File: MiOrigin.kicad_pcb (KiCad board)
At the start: 2 copper layers, 56.3 x 98 mm, 63 parts, among them J2 USB_C_Receptacle, J3 Micro_SD_Card, J4 CONN_02JST-PTH-2, J5 DB9_Male_MountingHoles, Q1 PMBT3904YS, Q2 DMG2305UX-13, Q5 DMG2305UX-13, U1 ESP32-WROOM-32U, U2 CH340C, U3 MCP73811T-420I-OT, U4 3.5-TFT-LCD-SPI, U5 AP2112K-3.3, U6 MAX1704X, U7 SN74LVC125ADBR_(Units), U8 MAX3232

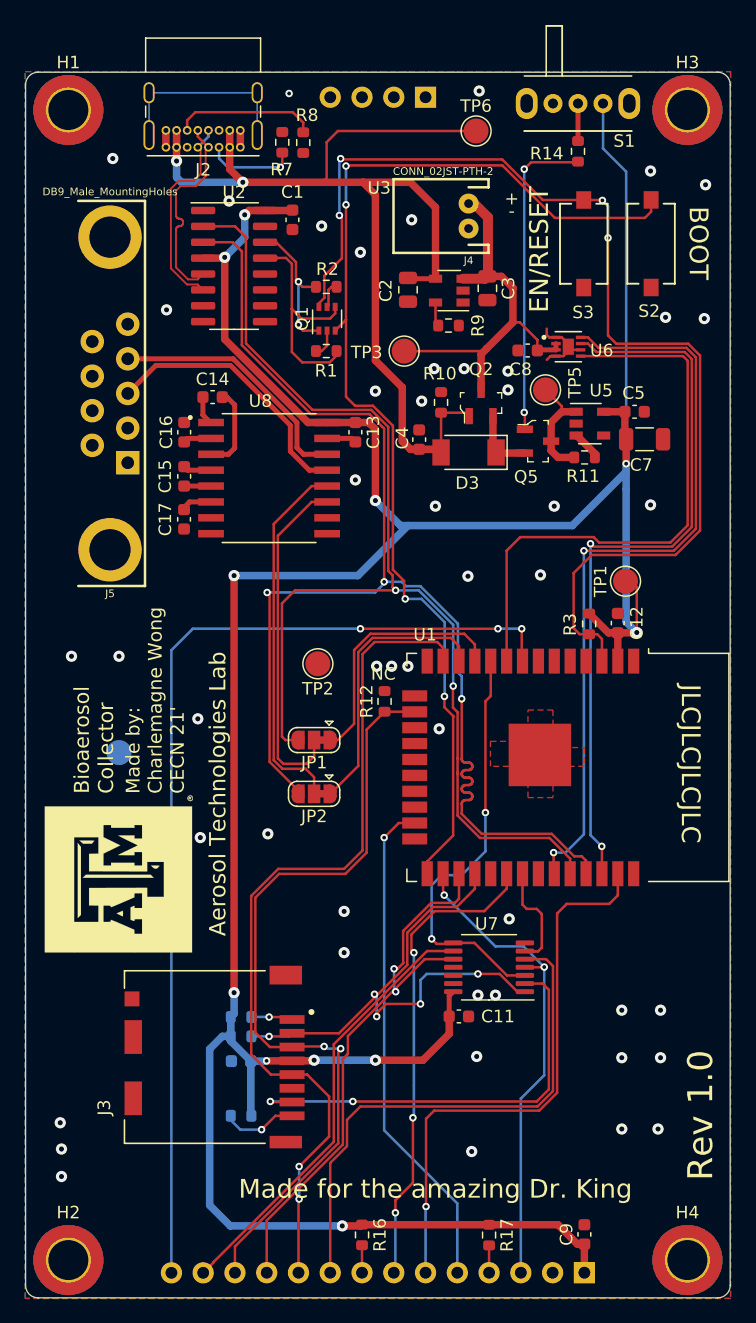
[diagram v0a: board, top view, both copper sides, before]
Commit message: Replace USB to UART with CP2102-GM
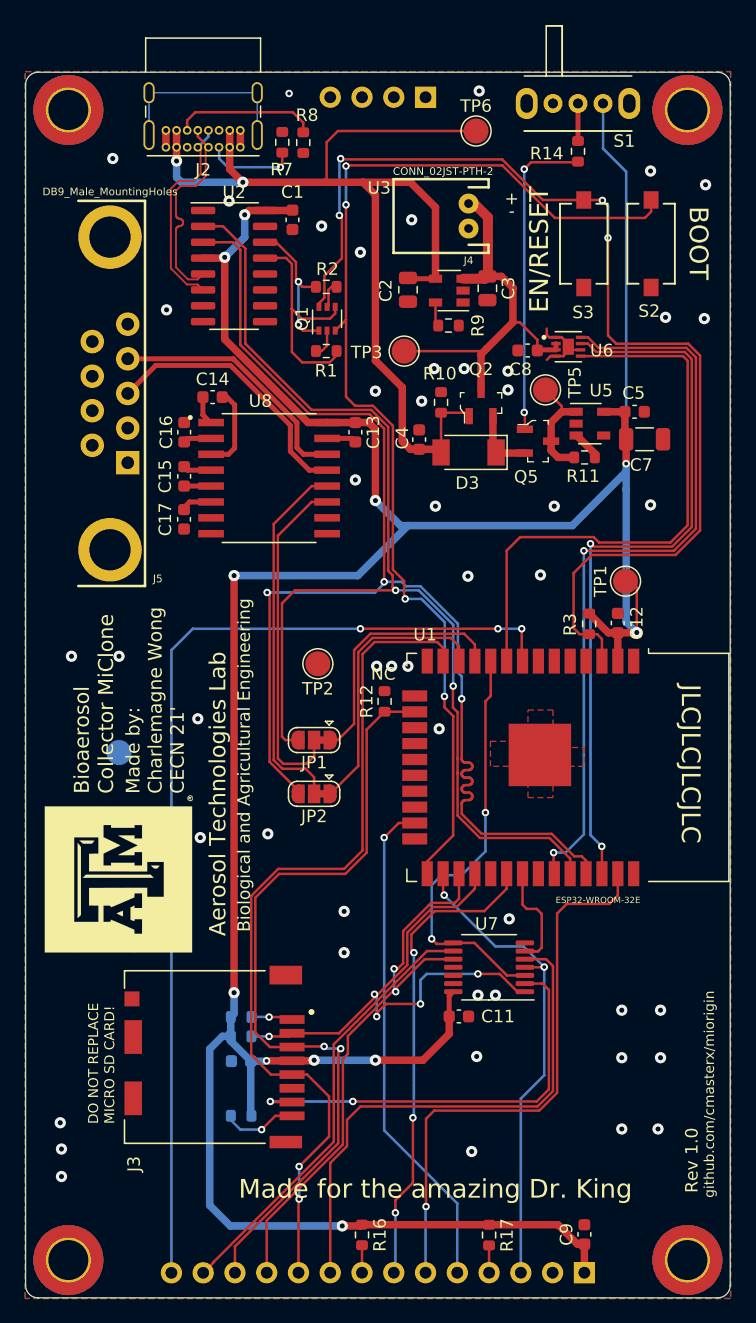
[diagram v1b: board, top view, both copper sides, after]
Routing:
- net CH340-TX: track 94.1 -> 93.6 mm
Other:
- board text added: "Bioaerosol Collector MiClone"
- board text added: "Biological and Agricultural Engineering"
- board text added: "DO NOT REPLACE MICRO SD CARD!"
- board text added: "ESP32-WROOM-32E"
- board text added: "github.com/cmasterx/miorigin"
- board text removed: "Bioaerosol Collector"

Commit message: Update board
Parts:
- added C10: 0.1uF, Capacitor_SMD:C_0603_1608Metric, F.Cu at (141.3, 57.5)
- added C18: 0.1uF, Capacitor_SMD:C_0603_1608Metric, F.Cu at (143.8, 61.2)
- added C19: 4.7uF, Capacitor_SMD:C_0805_2012Metric, F.Cu at (143.9, 59.4)
- added D1: SP0503BAHTG, digikey-footprints:SOT-143-4, F.Cu at (137.8, 57.1)
- C1: value 0.1uF -> 1uF; moved to B.Cu
- U1: value ESP32-WROOM-32U -> ESP32-WROOM-32E
- U2: value CH340C -> CP2102; footprint Package_SO:SOIC-16_3.9x9.9mm_P1.27mm -> CP2102:QFN50P500X500X100-29N
- U3: value MCP73811T-420I-OT -> MCP73832-2-OT
- moved C1 4.87 mm to (141.1, 57.1)
- moved U2 2.51 mm to (139.1, 62.2), turned to 180 degrees
- moved R8 2.24 mm to (146.1, 49.0), turned to 180 degrees
- moved R14 1.52 mm to (167.9, 53.1), turned to 180 degrees
- moved R7 1.03 mm to (146.1, 50.8), turned to 0 degrees
- moved G*** 0.46 mm to (132.5, 109.5)
- turned R1 to 0 degrees
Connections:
- C1 pad 1: GND -> +3V3
- C1 pad 2: +3V3 -> GND
- D3 pad 1: Net-(D3-Pad1) -> V_PREMOS
- Q2 pad 2: Net-(D3-Pad1) -> V_PREMOS
- Q5 pad 2: Net-(D3-Pad1) -> V_PREMOS
- S1 pad 1: +3V3 -> V_PREMOS
- U2 pad 1: GND -> Net-(U2-Pad1)
- U2 pad 13: CH340-DTR -> Net-(U2-Pad10)
- U2 pad 14: CH340-RTS -> Net-(U2-Pad10)
- U2 pad 15: Net-(U2-Pad15) -> Net-(U2-Pad10)
- U2 pad 16: +3V3 -> Net-(U2-Pad10)
- U2 pad 2: CH340-TX -> Net-(U2-Pad2)
- U2 pad 3: CH340-RX -> GND
- U2 pad 4: +3V3 -> D+
- U2 pad 5: D+ -> D-
- U2 pad 6: D- -> +3V3
- U2 pad 7: Net-(U2-Pad7) -> +3V3
- U2 pad 8: Net-(U2-Pad8) -> +VUSB_IN
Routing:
- net V_PREMOS: track 0.00 -> 37.6 mm, vias 0 -> 1
- net +3V3: track 248.5 -> 222.6 mm, vias 11 -> 10
- net +VUSB_IN: track 84.9 -> 97.3 mm, vias 2 -> 0
- net D-: track 16.5 -> 28.8 mm
- net D+: track 16.5 -> 25.9 mm, vias 0 -> 2
- net CH340-TX: track 93.6 -> 85.2 mm
- net CH340-RTS: track 12.1 -> 19.1 mm, vias 2 -> 3
- net GND: track 11.3 -> 17.6 mm, vias 49 -> 54
- net CH340-RX: track 103.0 -> 96.7 mm
- net Net-(D3-Pad1): track 5.32 -> 0.00 mm
- net Net-(J2-PadA5): track 7.33 -> 11.7 mm
- net Net-(J2-PadS1): track 15.4 -> 12.0 mm
- net Net-(J2-PadB5): track 11.5 -> 8.61 mm
- net CH340-DTR: track 18.4 -> 16.2 mm
- net Net-(R14-Pad1): track 3.00 -> 5.10 mm
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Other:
- rule via_min_drill: 0.3 -> 0.2
- rule via_min_size: 0.6 -> 0.4
- board text added: "Aerosol Technology Lab"
- board text removed: "Aerosol Technologies Lab"
